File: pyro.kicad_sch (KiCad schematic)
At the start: 21 parts, among them Q1 SI7232DN-T1-GE3, Q2 SI7232DN-T1-GE3, Q3 SI7232DN-T1-GE3

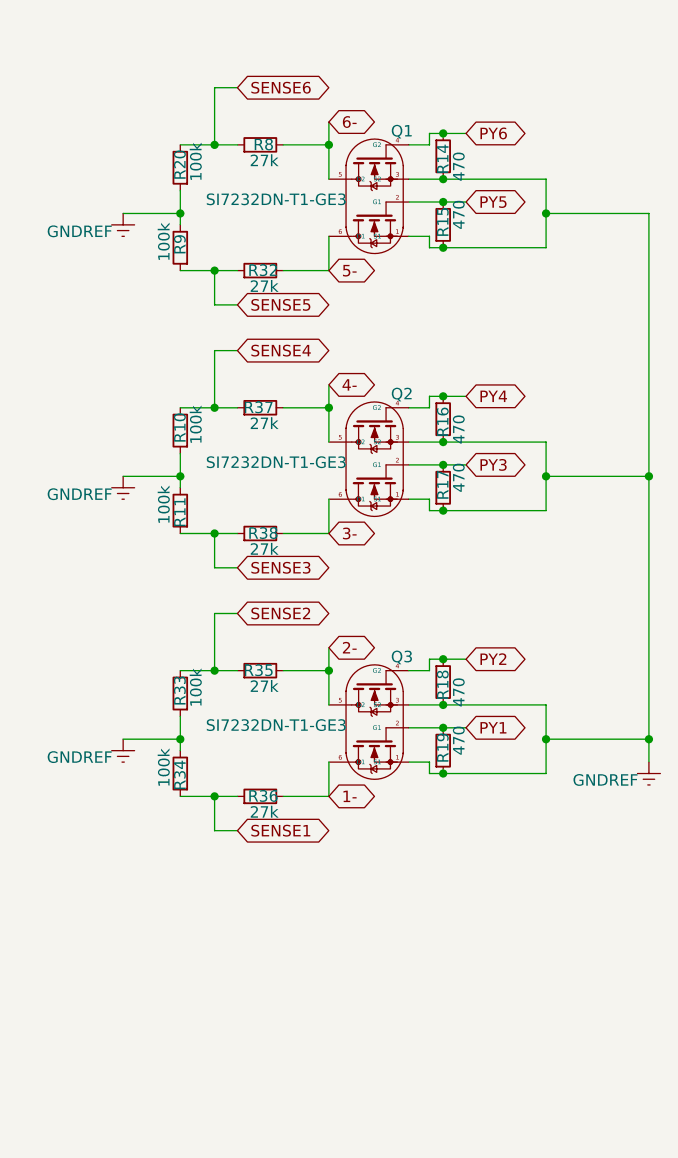
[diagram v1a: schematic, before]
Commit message: updated power delivery and component choices. v4 now ready
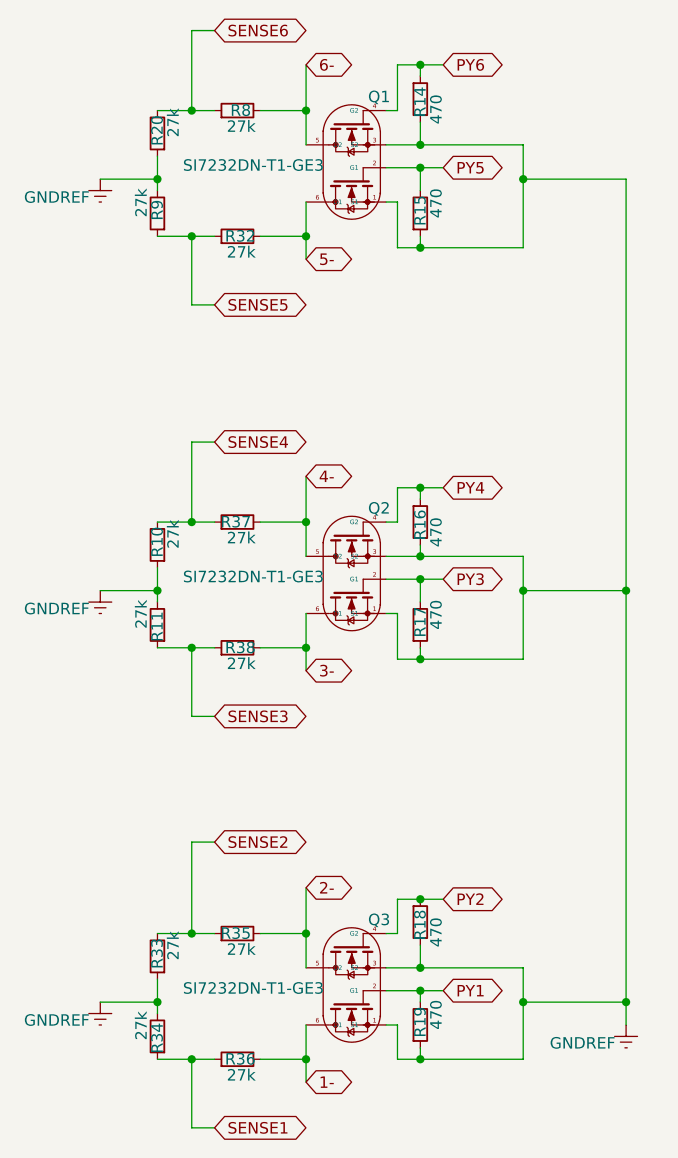
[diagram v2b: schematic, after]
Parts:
- R10, R11, R20, R33, R34, R9: value 100k -> 27k; Product ID RMCF0603FT100K -> RMCF0603JT27K0
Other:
- moved on the sheet: Q1, Q2, Q3, R10, R11, R14, R15, R16, R17, R18, R19, R20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
